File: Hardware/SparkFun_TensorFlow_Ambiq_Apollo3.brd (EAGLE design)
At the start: 40 x 40 mm, 132 parts, among them J5 CORTEX_DEBUG_PTH, J6 CAMERA-OV7670, M1 MEMS_MIC, M2 MEMS_MIC, U1 AMBIQ-APOLLO3KBR, U2 LIS2DH12, U3 1.8V, U4 LMV358, Y1 32MHz, Y2 32.768kHz

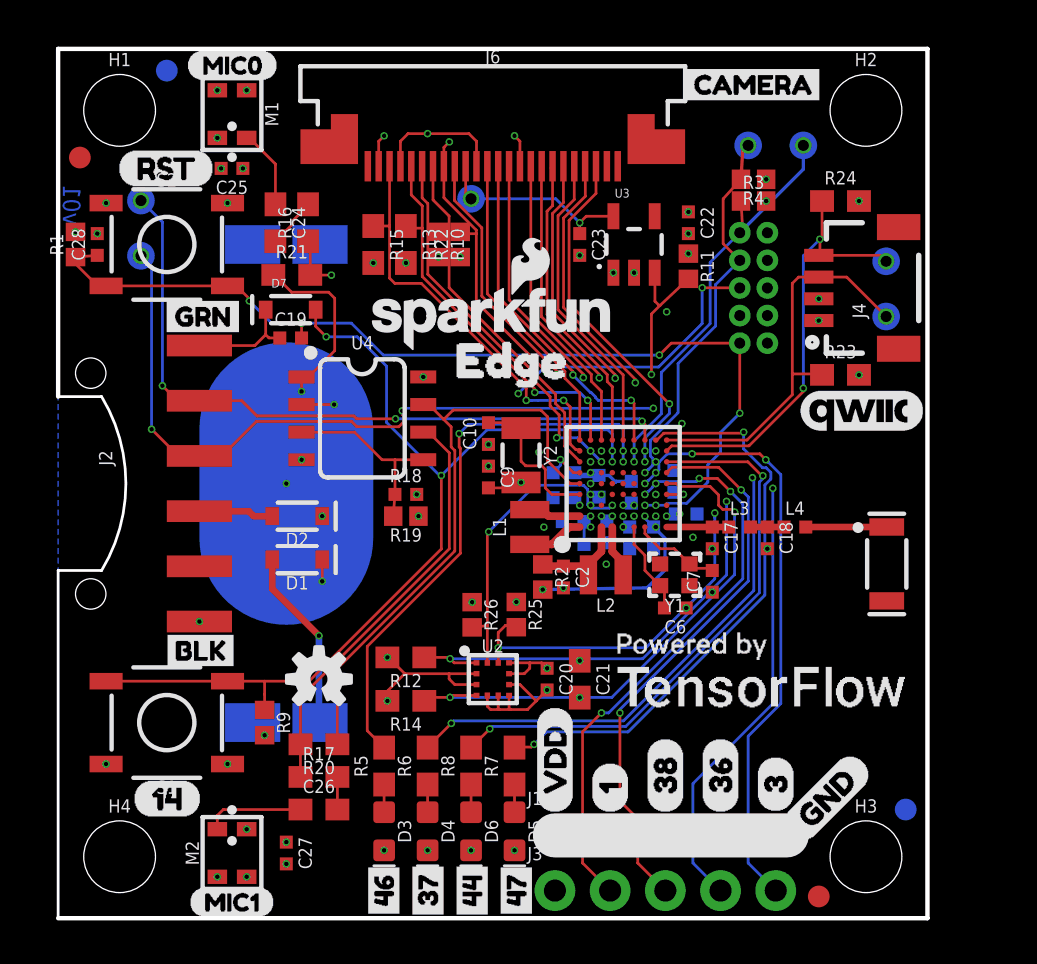
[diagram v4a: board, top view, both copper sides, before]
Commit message: Change to module layout
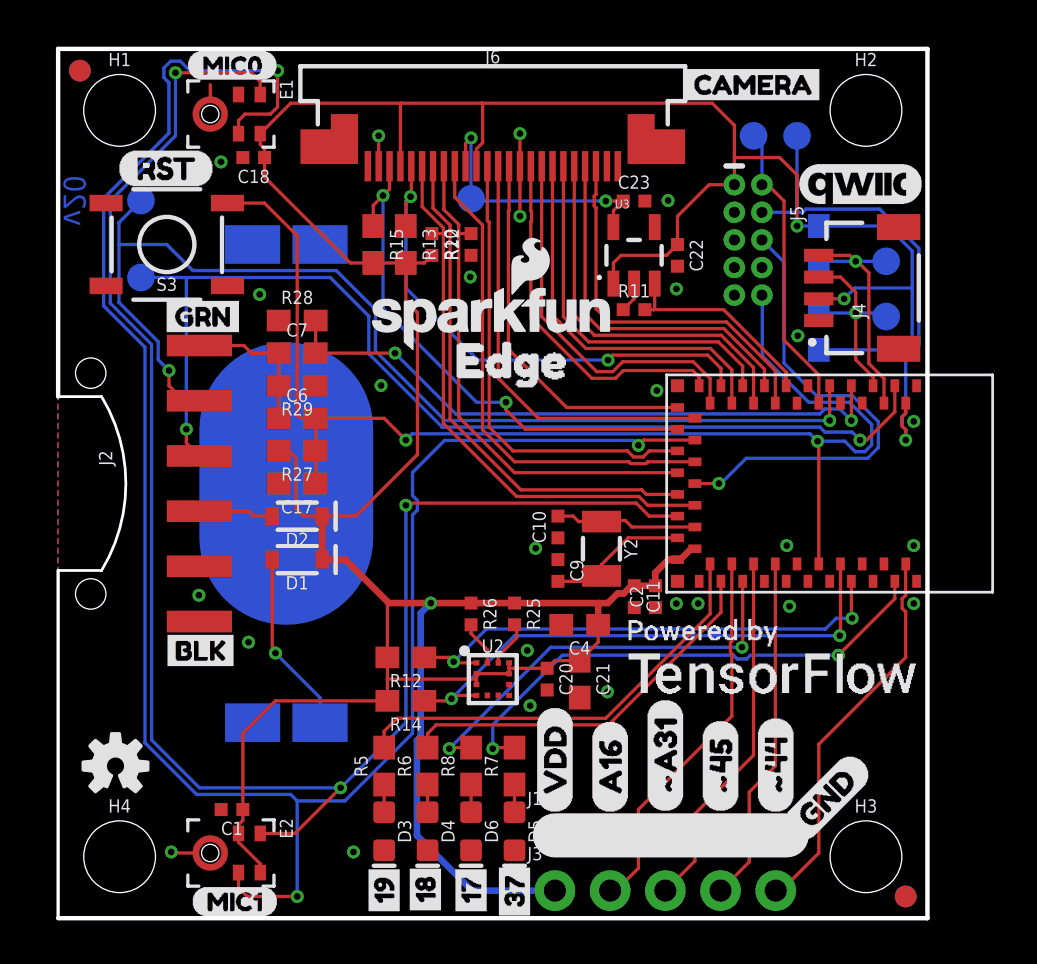
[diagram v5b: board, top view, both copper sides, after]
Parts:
- removed A1: 2.4GHZ-3.2X1.6MM, ambiq:ANT-2.4GHZ-3.2X1.6X1.2MM
- removed C12, C13, C14, C15: 1.0uF, ambiq:0402-TIGHT
- removed C16, C3, C5, C8: 2.2uF, SparkFun-Capacitors:0402-TIGHT
- removed C19, C25, C27: 0.1uF, ambiq:0402-TIGHT
- removed C24, C26: 4.7uF, SparkFun-Capacitors:0603
- removed C28: 1.0nF, SparkFun-Capacitors:0402-TIGHT
- removed D7: DNP, SparkFun-DiscreteSemi:SOD-323
- removed L1: 2.2μH, SparkFun-Coils:0805-WIDE
- removed L2: 1.0μH, SparkFun-Coils:0805-WIDE
- removed L3: 2.7nH/?%/900mA/70mOhm, SparkFun-Coils:0402-TIGHT
- removed L4: 2nH/?%/200mA/300mOhm, SparkFun-Coils:0402-TIGHT
- removed M1, M2: MEMS_MIC, SparkFun-Sensors:SPW2430HR5H-B
- removed R1, R19, R3, R4: 10k, SparkFun-Resistors:0402
- removed R16, R17: 10k, SparkFun-Resistors:0603
- removed R18: 22k, SparkFun-Resistors:0402-TIGHT
- removed R2: 0, SparkFun-Resistors:0402
- removed R20, R21: 750K, SparkFun-Resistors:0603
- removed R9: 100k, SparkFun-Resistors:0402
- removed S1: (no value), SparkFun-Switches:TACTILE_SWITCH_SMD_5.2MM
- removed U$15: (no value), buzzard_labels:461
- removed U$17: (no value), buzzard_labels:443
- removed U$18: (no value), buzzard_labels:470
- removed U$22: (no value), buzzard_labels:MIC11
- removed U1: AMBIQ-APOLLO3KBR, SparkFun-IC-Microcontroller:BGA-81-5X5MM
- removed U4: LMV358, SparkFun-IC-Amplifiers:SO08
- removed Y1: 32MHz, SparkFun-Clocks:CRYSTAL-SMD-2.0X1.6MM
- added E1, E2: SPH0641LM4H-1, SparkFun-Sensors:SPH0641LM4H-1_MICROPHONE
- added R27, R29: 100k, SparkFun-Resistors:0603
- added R28: 10k, SparkFun-Resistors:0603
- added U$31: (no value), buzzard_labels (14):193
- added U$32: (no value), buzzard_labels (11):EDGE_20
- added U$36: (no value), buzzard_labels (9):#444
- added U5: ARTEMIS_MODULESMD, Testing:ARTEMIS_FP
- C1: value 0.47uF -> 0.1uF; device SparkFun-Capacitors:0402-TIGHT -> ambiq:0402-TIGHT
- C11: value 47nF -> 1.0uF
- C17: value DNP -> 1nF; device ambiq:0402-TIGHT -> SparkFun-Capacitors:0603
- C18: value 0.5pF -> 0.1uF; device SparkFun-Capacitors:0402-TIGHT -> ambiq:0402-TIGHT
- C2: value 4.7uF -> 0.1uF
- C4: value 1.0uF -> 10uF; device ambiq:0402-TIGHT -> SparkFun-Capacitors:0603
- C6: value 6pF -> 0.1uF; device ambiq:0402-TIGHT -> SparkFun-Capacitors:0603
- C7: value 6pF -> 2.2uF; device ambiq:0402-TIGHT -> SparkFun-Capacitors:0603
- D1, D2: device SparkFun-DiscreteSemi:SOD-323@1 -> SparkFun-DiscreteSemi:SOD-323
- J4: device SparkFun-Connectors:1X04_1MM_RA -> SparkFun-Connectors:JST04_1MM_RA
- J5: value CORTEX_DEBUG_PTH -> CORTEX_DEBUG; device SparkFun-Connectors:2X5-PTH-1.27MM -> SparkFun-Connectors:2X5-PTH-1.27MM-NO_SILK
- R10, R11, R22, R25, R26: device SparkFun-Resistors:0402 -> SparkFun-Resistors:0402-TIGHT
- S3: value (none) -> RESET
- TP1, TP2: value TEST-POINT3X5 -> (none)
- U$10: device buzzard_labels:31 -> buzzard_labels (9):A161
- U$11, U$6: device buzzard_labels:383 -> buzzard_labels (9):#A312
- U$12: device buzzard_labels:364 -> buzzard_labels (9):#453
- U$13: device buzzard_labels:31 -> buzzard_labels (9):#444
- U$23: device buzzard_labels:EDGE0 -> buzzard_labels (13):171
- U$26: device buzzard_labels:1416 -> buzzard_labels (14):182
- U$5: device buzzard_labels:10 -> buzzard_labels (9):#453
- U$7: device buzzard_labels:364 -> buzzard_labels (9):A161
- U$8: device buzzard_labels:10 -> buzzard_labels (9):MIC10
- moved U$23 35.4 mm to (19.0, -0.10), flipped to the top, turned to 90 degrees
- moved C18 29.4 mm to (9.00, 35.0), turned to 180 degrees
- moved U$30 29.3 mm to (2.64, 7.00)
- moved C7 21.8 mm to (11.0, 26.0), turned to 0 degrees
- moved C1 21.8 mm to (8.00, 5.00), flipped to the top
- moved U$8 19.7 mm to (6.10, 0.76), flipped to the top, turned to 0 degrees
- moved C6 19.5 mm to (11.0, 23.0), turned to 0 degrees
- moved C17 19.3 mm to (11.0, 20.0), turned to 180 degrees
- moved U$26 14.6 mm to (16.9, -0.10), turned to 90 degrees
- moved U$19 10.4 mm to (36.9, 33.8)
- moved LOGO2 10.2 mm to (2.64, 7.00)
- moved U$10 7.62 mm to (25.4, 4.83)
- moved Y2 5.67 mm to (25.0, 17.0)
- moved C10 5.36 mm to (23.0, 18.0)
- moved C9 5.36 mm to (23.0, 16.0)
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- renumbered S2 to S3
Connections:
- removed net ADC_VREF: C1.1, U1.A6
- removed net DTR: C19.1, D7.C, J2.1
- removed net DVDD: C11.1, U1.H3
- removed net GPIO0/ACCEL_INT2: R25.2, U1.H4, U2.11
- removed net GPIO10/CAMERA_DVDD_EN: R11.2, U1.G8, U3.3
- removed net GPIO11/MIC0: R21.1, U1.B5, U4.1
- removed net GPIO12/CAMERA_VSYNC: J6.7, U1.A7
- removed net GPIO13/CAMERA_PWDN: J6.8, R22.2, U1.B7
- removed net GPIO14/USER_BUTTON: D7.A, R9.1, S1.3, S1.4, U1.D7
- removed net GPIO15/CAMERA_RESET: J6.6, R10.1, U1.C7
- removed net GPIO17/ACCEL_INT1: R26.2, U1.D3, U2.12
- removed net GPIO1_J3_2: J3.2, U1.G4
- removed net GPIO20/SWDCK: J5.4, R4.2, TP1.P$1, U1.G6
- removed net GPIO21/SWDIO: J5.2, R3.1, TP2.P$1, U1.F7
- removed net GPIO22/CAMERA_Y5: J6.16, U1.C9
- removed net GPIO23/CAMERA_PCLK: J6.17, U1.D8
- removed net GPIO24/CAMERA_Y6: J6.14, U1.C8
- removed net GPIO25/I2C_SDA_CAMERA: J6.3, R15.1, U1.A8
- removed net GPIO26/CAMERA_HREF: J6.9, U1.B8
- removed net GPIO27/I2C_SCL_CAMERA: J6.5, R13.1, U1.B9
- removed net GPIO28/CAMERA_Y7: J6.12, U1.A9
- removed net GPIO29/MIC1: R20.1, U1.A5, U4.7
- removed net GPIO33/SWO: J5.6, U1.B6
- removed net GPIO36_J3_4: J3.4, U1.H6
- removed net GPIO37_LED_BLUE: R6.2, U1.H7
- removed net GPIO38_J3_3: J3.3, U1.J6
- removed net GPIO39_QWIIC_SCK: J4.4, R24.1, TP3.P$1, U1.J8
- removed net GPIO3_J3_5: J3.5, U1.G5
- removed net GPIO4/CAMERA_Y4: J6.18, U1.D9
- removed net GPIO40_QWIIC_SDA: J4.3, R23.1, TP4.P$1, U1.J9
- removed net GPIO42/I2C_SCLK: R12.1, U1.H5, U2.1
- removed net GPIO43/I2C_SDA: R14.1, U1.J5, U2.4
- removed net GPIO44/LED_GREEN: R8.2, U1.J7
- removed net GPIO46/LED_RED: R5.2, U1.E7
- removed net GPIO47/LED_YELLOW: R7.2, U1.H9
- removed net GPIO5/CAMERA_Y3: J6.20, U1.E9
- removed net GPIO6/CAMERA_Y0: J6.19, U1.E8
- removed net GPIO7/CAM_XCLK: J6.13, U1.F9
- removed net GPIO8/CAMERA_Y1: J6.21, U1.F8
- removed net GPIO9/CAMERA_Y2: J6.22, U1.G7
- removed net MIC0_OUT: C24.1, M1.1
- removed net MIC1_OUT: C26.1, M2.1
- removed net N$1: A1.FEED, L4.2
- removed net N$10: C24.2, R16.2
- removed net N$11: R17.1, R20.2, U4.6
- removed net N$12: R16.1, R21.2, U4.2
- removed net N$14: C26.2, R17.2
- removed net N$16: C18.1, L3.2, L4.1
- removed net N$3: C6.2, U1.F1, Y1.3
- removed net N$9: R18.1, R19.2, U4.3, U4.5
- removed net RFIOP: C17.1, L3.1, U1.J1
- removed net SIMBUCK_SWSEL: L1.2, U1.A2
- removed net SIMOBUCK_SW: L1.1, U1.A1
- removed net UART-RX/GPIO49: J2.3, TP6.P$1, U1.H8
- removed net UART-TX/GPIO48: J2.2, TP5.P$1, U1.G9
- removed net VDCDCRF: C4.1, R2.2, U1.G2
- removed net VDDBH: C2.1, L2.2, R2.1, U1.C1
- removed net VDDBH_SW: L2.1, U1.D1
- removed net VDDC: C3.1, U1.A3
- removed net VDDF: C5.1, U1.D2
- removed net VDDS: C8.1, U1.E1
- removed net XI: C9.2, U1.B4, Y2.P$2
- new net !DTR: C6.1, C7.1, J2.1, R29.2
- new net A16: J3.2, U5.AD16
- new net ACCEL_I2C_SCL: R12.1, U2.1, U5.~D42
- new net ACCEL_I2C_SDA: R14.1, U2.4, U5.~D43
- new net ACCEL_INT1: R26.2, U2.12
- new net ACCEL_INT2: R25.2, U2.11
- new net BOOT: C7.2, R28.2, U5.BOOT
- new net CAMERA_DVDD_EN: R11.2, U3.3, U5.D7
- new net CAMERA_HREF: J6.9, U5.~AD13
- new net CAMERA_I2C_SCL: J6.5, R13.1, U5.~D27
- new net CAMERA_I2C_SDA: J6.3, R15.1, U5.~D25
- new net CAMERA_PCLK: J6.17, U5.D14
- new net CAMERA_PWDN: J6.8, R22.2, U5.D15
- new net CAMERA_RESET: J6.6, R10.1, U5.~AD11
- new net CAMERA_VSYNC: J6.7, U5.AD34
- new net CAMERA_XCLK: J6.13, U5.~AD32
- new net CAMERA_Y0: J6.19, U5.~D22
- new net CAMERA_Y1: J6.21, U5.~D4
- new net CAMERA_Y2: J6.22, U5.~AD35
- new net CAMERA_Y3: J6.20, U5.~D24
- new net CAMERA_Y4: J6.18, U5.~D23
- new net CAMERA_Y5: J6.16, U5.~D28
- new net CAMERA_Y6: J6.14, U5.~D6
- new net CAMERA_Y7: J6.12, U5.~D26
- new net LED_BLUE: R6.2, U5.~D18
- new net LED_GREEN: R8.2, U5.D17
- new net LED_RED: R5.2, U5.~D19
- new net LED_YELLOW: R7.2, U5.~D37
- new net MIC_CLK: E1.4, E2.4, U5.~AD12
- new net MIC_DATA: E1.1, E2.1, U5.~AD29
- new net QWIIC_SCL: J4.4, R24.1, TP3.P$1, U5.~D39
- new net QWIIC_SDA: J4.3, R23.1, TP4.P$1, U5.D40
- new net SWDCK: J5.4, TP1.P$1, U5.SWDCK
- new net SWDIO: J5.2, TP2.P$1, U5.SWDIO
- new net UART-RX: J2.3, TP6.P$1, U5.RXI-0
- new net UART-TX: J2.2, TP5.P$1, U5.TXO-0
- new net ~44: J3.5, U5.~D44
- new net ~45: J3.4, U5.~D45
- new net ~A31: J3.3, U5.~AD31
- new net ~AD33/SWO: J5.6, U5.~AD33/SWO
- net AMBIQ_!RST: now also C17.1, C6.2, R27.1, U5.~RST; no longer C19.2, C28.1, R1.1, S3.4, U1.G3
- net GND: now also C2.1, E1.2, E1.3, E1.6, E1.7, E1.8, E2.3, E2.6, E2.7, E2.8, R28.1, R29.1, U5.GND@1, U5.GND@22, U5.GND@38, U5.GND@39, U5.GND@47, U5.GND@59; no longer C12.2, C13.2, C14.2, C15.2, C16.2, C2.2, C25.2, C27.2, C28.2, C3.2, C5.2, C6.1, C7.1, C8.2, M1.2, M1.3, M2.2, M2.3, R19.1, R4.1, S1.1, S1.2, S3.2, U1.B3, U1.C2, U1.E2, U1.E3, U1.F2, U1.H1, U1.H2, U1.J2, U4.4
- net N$2: now also C9.2, U5.XI, Y2.P$2; no longer C7.2, U1.G1, Y1.1
- net VDD: now also C1.1, C11.1, C18.1, C2.2, C4.1, E1.5, E2.2, E2.5, R27.2, U5.VDD@36, U5.VDD@37; no longer C12.1, C13.1, C14.1, C15.1, C16.1, C25.1, C27.1, M1.4, M2.4, R1.2, R18.2, R3.2, R9.2, U1.B1, U1.B2, U1.C4, U1.F3, U1.J4, U4.8
- net X0: now also U5.XO; no longer U1.A4
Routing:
- net VDD: track 21.8 -> 167.0 mm, vias 31 -> 3
- net MIC_CLK: track 0.00 -> 91.7 mm, vias 0 -> 3
- net MIC_DATA: track 0.00 -> 78.6 mm, vias 0 -> 3
- net UART-TX: track 0.00 -> 50.3 mm, vias 0 -> 2
- net UART-RX: track 0.00 -> 49.0 mm, vias 0 -> 2
- net GPIO14/USER_BUTTON: track 43.7 -> 0.00 mm, vias 3 -> 0
- net UART-RX/GPIO49: track 35.3 -> 0.00 mm, vias 5 -> 0
- net UART-TX/GPIO48: track 32.6 -> 0.00 mm, vias 4 -> 0
- net BOOT: track 0.00 -> 29.2 mm, vias 0 -> 2
- net GPIO37_LED_BLUE: track 28.0 -> 0.00 mm, vias 3 -> 0
- net GPIO29/MIC1: track 27.9 -> 0.00 mm
- net GPIO3_J3_5: track 27.7 -> 0.00 mm, vias 3 -> 0
- net GPIO1_J3_2: track 26.9 -> 0.00 mm, vias 4 -> 0
- net GPIO47/LED_YELLOW: track 26.9 -> 0.00 mm, vias 2 -> 0
- net GPIO36_J3_4: track 26.5 -> 0.00 mm, vias 2 -> 0
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- added copper zone on layer 1, net GND
- removed copper zone on layer 15, net CUTOUT
- removed copper zone on layer 2, net CUTOUT
- removed copper zone on layer 2, net GND
- removed copper zone on layer 15, net VDD
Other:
- board text added: "v20"
- board text removed: "This is a 4-layer board!"
- board text removed: "v01"

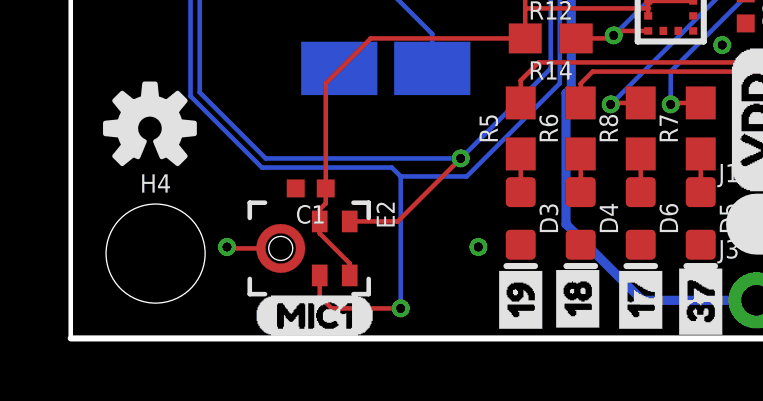
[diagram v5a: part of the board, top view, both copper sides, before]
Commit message: Update SparkFun_TensorFlow_Ambiq_Apollo3.brd
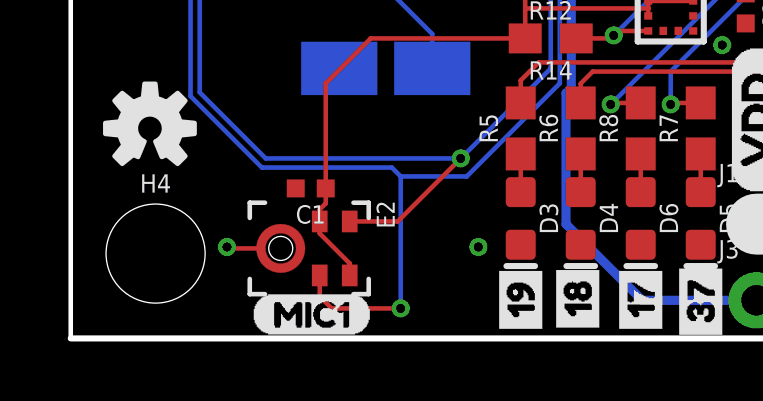
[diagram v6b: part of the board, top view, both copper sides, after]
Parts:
- moved U$8 0.10 mm to (6.00, 0.80)
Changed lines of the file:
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@@
 <element name="U$6" library="buzzard_labels (9)" package="#A312" value="" x="27.94" y="4.826" smashed="yes" rot="R90"/>
 <element name="U$7" library="buzzard_labels (9)" package="A161" value="" x="25.4" y="4.826" smashed="yes" rot="R90"/>
-<element name="U$8" library="buzzard_labels (9)" package="MIC10" value="" x="6.096" y="0.762" smashed="yes"/>
+<element name="U$8" library="buzzard_labels (9)" package="MIC10" value="" x="6" y="0.8" smashed="yes"/>
 <element name="U$10" library="buzzard_labels (9)" package="A161" value="" x="25.4" y="4.826" smashed="yes" rot="MR90"/>
 <element name="U$11" library="buzzard_labels (9)" package="#A312" value="" x="27.94" y="4.826" smashed="yes" rot="MR90"/>

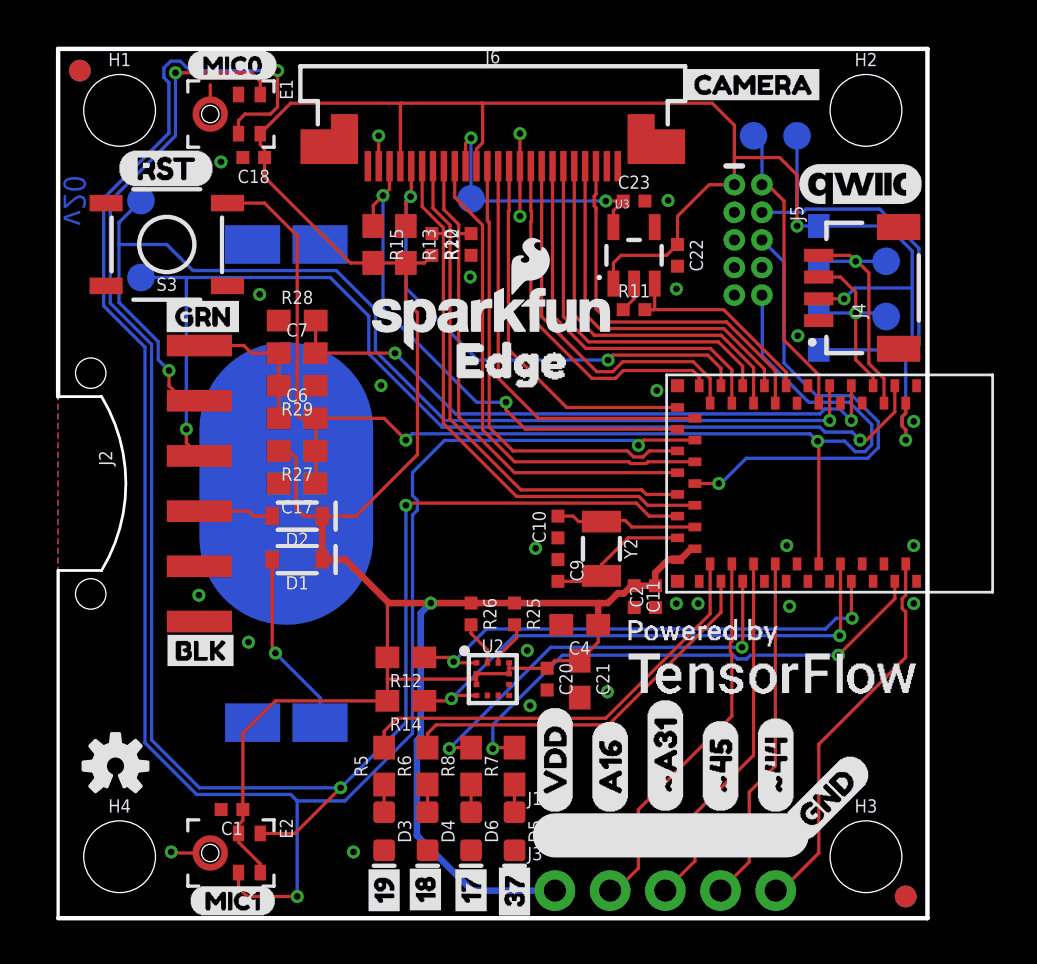
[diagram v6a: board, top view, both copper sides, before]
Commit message: Moving TP to align with jig.
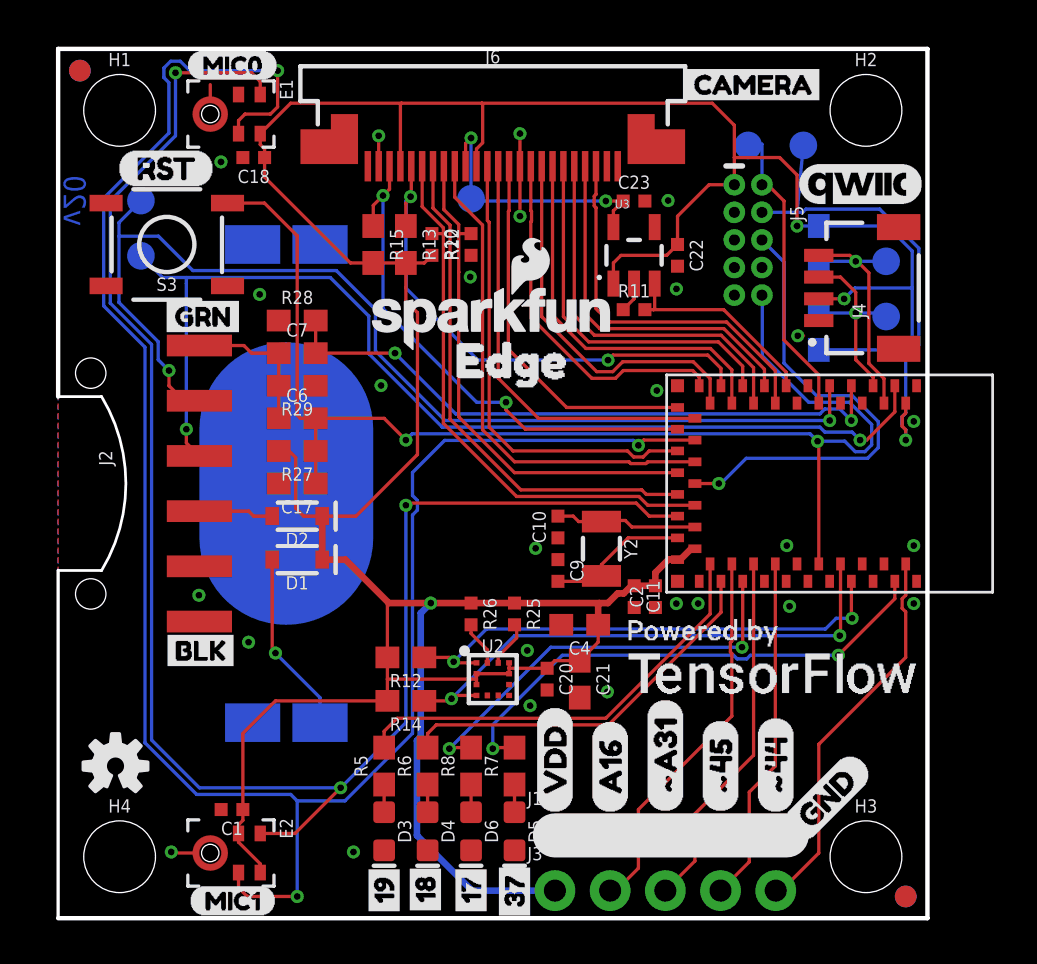
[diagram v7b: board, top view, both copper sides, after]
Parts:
- moved TP6 1.00 mm to (3.81, 30.5)
- moved TP1 0.53 mm to (34.3, 35.6)
- moved TP2 0.51 mm to (31.8, 35.6)
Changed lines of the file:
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@@
 <setting verticaltext="up"/>
 </settings>
-<grid distance="1" unitdist="mm" unit="mm" style="lines" multiple="1" display="yes" altdistance="0.1" altunitdist="mm" altunit="mm"/>
+<grid distance="0.05" unitdist="inch" unit="inch" style="lines" multiple="1" display="yes" altdistance="0.005" altunitdist="inch" altunit="inch"/>
 <layers>
 <layer number="1" name="Top" color="4" fill="1" visible="yes" active="yes"/>
@@
 <layer number="47" name="Measures" color="7" fill="1" visible="no" active="yes"/>
 <layer number="48" name="Document" color="7" fill="1" visible="no" active="yes"/>
-<layer number="49" name="Reference" color="7" fill="1" visible="yes" active="yes"/>
+<layer number="49" name="Reference" color="7" fill="1" visible="no" active="yes"/>
 <layer number="50" name="dxf" color="7" fill="1" visible="no" active="yes"/>
 <layer number="51" name="tDocu" color="6" fill="1" visible="yes" active="yes"/>
@@
 <element name="U$24" library="buzzard_labels" package="EDGE0" value="" x="16.891" y="25.654" smashed="yes"/>
 <element name="U$1" library="buzzard_labels" package="MIC00" value="" x="5.9182" y="39.243" smashed="yes"/>
-<element name="TP1" library="SparkFun-Connectors" package="PAD.03X.05" value="" x="34" y="36" smashed="yes" rot="MR0"/>
-<element name="TP2" library="SparkFun-Connectors" package="PAD.03X.05" value="" x="32" y="36" smashed="yes" rot="MR0"/>
+<element name="TP1" library="SparkFun-Connectors" package="PAD.03X.05" value="" x="34.29" y="35.56" smashed="yes" rot="MR0"/>
+<element name="TP2" library="SparkFun-Connectors" package="PAD.03X.05" value="" x="31.75" y="35.56" smashed="yes" rot="MR0"/>
 <element name="TP3" library="SparkFun-Connectors" package="PAD.03X.05" value="TEST-POINT3X5" x="38.1" y="30.226" smashed="yes" rot="MR0"/>
 <element name="TP4" library="SparkFun-Connectors" package="PAD.03X.05" value="TEST-POINT3X5" x="38.1" y="27.686" smashed="yes" rot="MR0"/>
 <element name="TP5" library="SparkFun-Connectors" package="PAD.03X.05" value="TEST-POINT3X5" x="3.81" y="33.02" smashed="yes" rot="MR0"/>
-<element name="TP6" library="SparkFun-Connectors" package="PAD.03X.05" value="TEST-POINT3X5" x="3.81" y="29.48" smashed="yes" rot="MR0"/>
+<element name="TP6" library="SparkFun-Connectors" package="PAD.03X.05" value="TEST-POINT3X5" x="3.81" y="30.48" smashed="yes" rot="MR0"/>
 <element name="TP7" library="SparkFun-Connectors" package="PAD.03X.05" value="TEST-POINT3X5" x="19" y="33.1016" smashed="yes" rot="MR0"/>
 <element name="U$25" library="PoweredBy_TF#jpg" package="POWEREDBY_TF#JPG" value="" x="13.335" y="6.223" smashed="yes" rot="MR0"/>
@@
 <wire x1="37.80245625" y1="32.6286" x2="34.4053125" y2="32.6286" width="0.1524" layer="16"/>
 <wire x1="39.6048" y1="30.82625625" x2="37.80245625" y2="32.6286" width="0.1524" layer="16"/>
-<wire x1="34" y1="36" x2="34" y2="32.48" width="0.1524" layer="16"/>
+<wire x1="34.29" y1="35.56" x2="34" y2="32.48" width="0.1524" layer="16"/>
 <wire x1="39" y1="23.24434375" x2="39" y2="23.7" width="0.1524" layer="1"/>
 <wire x1="39" y1="23.24434375" x2="38.8366" y2="23.08094375" width="0.1524" layer="1"/>
@@
 <wire x1="35" y1="23.7" x2="35" y2="25" width="0.1524" layer="1"/>
 <wire x1="32.385" y1="33.75" x2="32.385" y2="35.615" width="0.1524" layer="16"/>
-<wire x1="32.385" y1="35.615" x2="32" y2="36" width="0.1524" layer="16"/>
+<wire x1="32.385" y1="35.615" x2="31.75" y2="35.56" width="0.1524" layer="16"/>
 <wire x1="33.4" y1="26.6" x2="33.4" y2="33" width="0.1524" layer="1"/>
 <wire x1="33.4" y1="33" x2="32.65" y2="33.75" width="0.1524" layer="1"/>
@@
 <wire x1="5.9" y1="21.87" x2="5.9" y2="22.5" width="0.1524" layer="1"/>
 <via x="5.9" y="22.5" extent="1-16" drill="0.3048"/>
-<wire x1="5.9" y1="22.5" x2="5.9" y2="29.48" width="0.1524" layer="16"/>
+<wire x1="5.9" y1="22.5" x2="5.9" y2="29.21" width="0.1524" layer="16"/>
+<wire x1="5.9" y1="29.21" x2="5.9" y2="29.48" width="0.1524" layer="16"/>
 <wire x1="14.2952" y1="27.7048" x2="12.52" y2="29.48" width="0.1524" layer="16"/>
-<wire x1="12.52" y1="29.48" x2="5.9" y2="29.48" width="0.1524" layer="16"/>
-<wire x1="5.9" y1="29.48" x2="3.81" y2="29.48" width="0.1524" layer="16"/>
+<wire x1="12.52" y1="29.48" x2="6.35" y2="29.48" width="0.1524" layer="16"/>
+<wire x1="6.35" y1="29.48" x2="5.9" y2="29.48" width="0.1524" layer="16"/>
+<wire x1="5.9" y1="29.48" x2="4.81" y2="29.48" width="0.1524" layer="16"/>
+<wire x1="4.81" y1="29.48" x2="3.81" y2="30.48" width="0.1524" layer="16"/>
 </signal>
 <signal name="UART-TX">
@@
 <wire x1="4.6048" y1="26.52625625" x2="2.8" y2="28.33105625" width="0.1524" layer="16"/>
 <wire x1="2.8" y1="32.01" x2="3.81" y2="33.02" width="0.1524" layer="16"/>
-<wire x1="2.8" y1="28.33105625" x2="2.8" y2="31" width="0.1524" layer="16"/>
-<wire x1="2.8" y1="31" x2="2.8" y2="32.01" width="0.1524" layer="16"/>
+<wire x1="2.8" y1="28.33105625" x2="2.8" y2="31.381" width="0.1524" layer="16"/>
+<wire x1="2.8" y1="31.381" x2="2.8" y2="32.01" width="0.1524" layer="16"/>
 <wire x1="14.6" y1="28" x2="12.8" y2="29.8" width="0.1524" layer="16"/>
-<wire x1="6.2" y1="29.8" x2="5" y2="31" width="0.1524" layer="16"/>
-<wire x1="5" y1="31" x2="2.8" y2="31" width="0.1524" layer="16"/>
+<wire x1="6.2" y1="29.8" x2="4.619" y2="31.381" width="0.1524" layer="16"/>
+<wire x1="4.619" y1="31.381" x2="2.8" y2="31.381" width="0.1524" layer="16"/>
 <wire x1="12.8" y1="29.8" x2="6.2" y2="29.8" width="0.1524" layer="16"/>
 </signal>
